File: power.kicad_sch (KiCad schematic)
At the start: 44 parts, among them U14 BH-18650-B5BA016, U2 SS-12D10L5, U4 TPS562209DDCR, U5 FXL0530-4R7-M

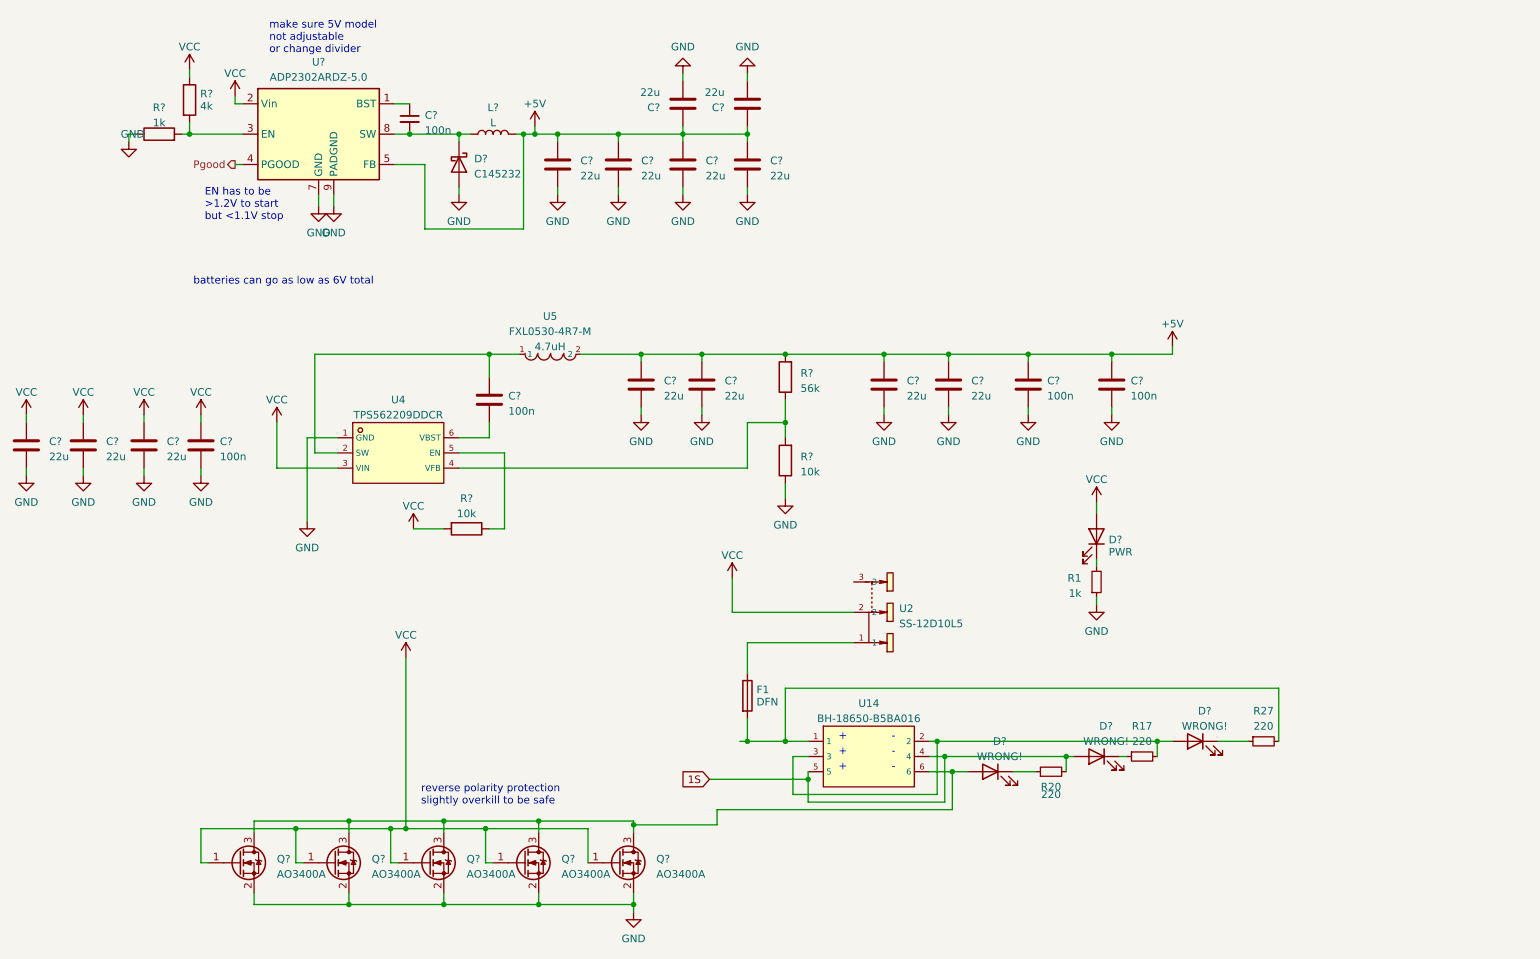
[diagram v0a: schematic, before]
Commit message: removed all dc to dc
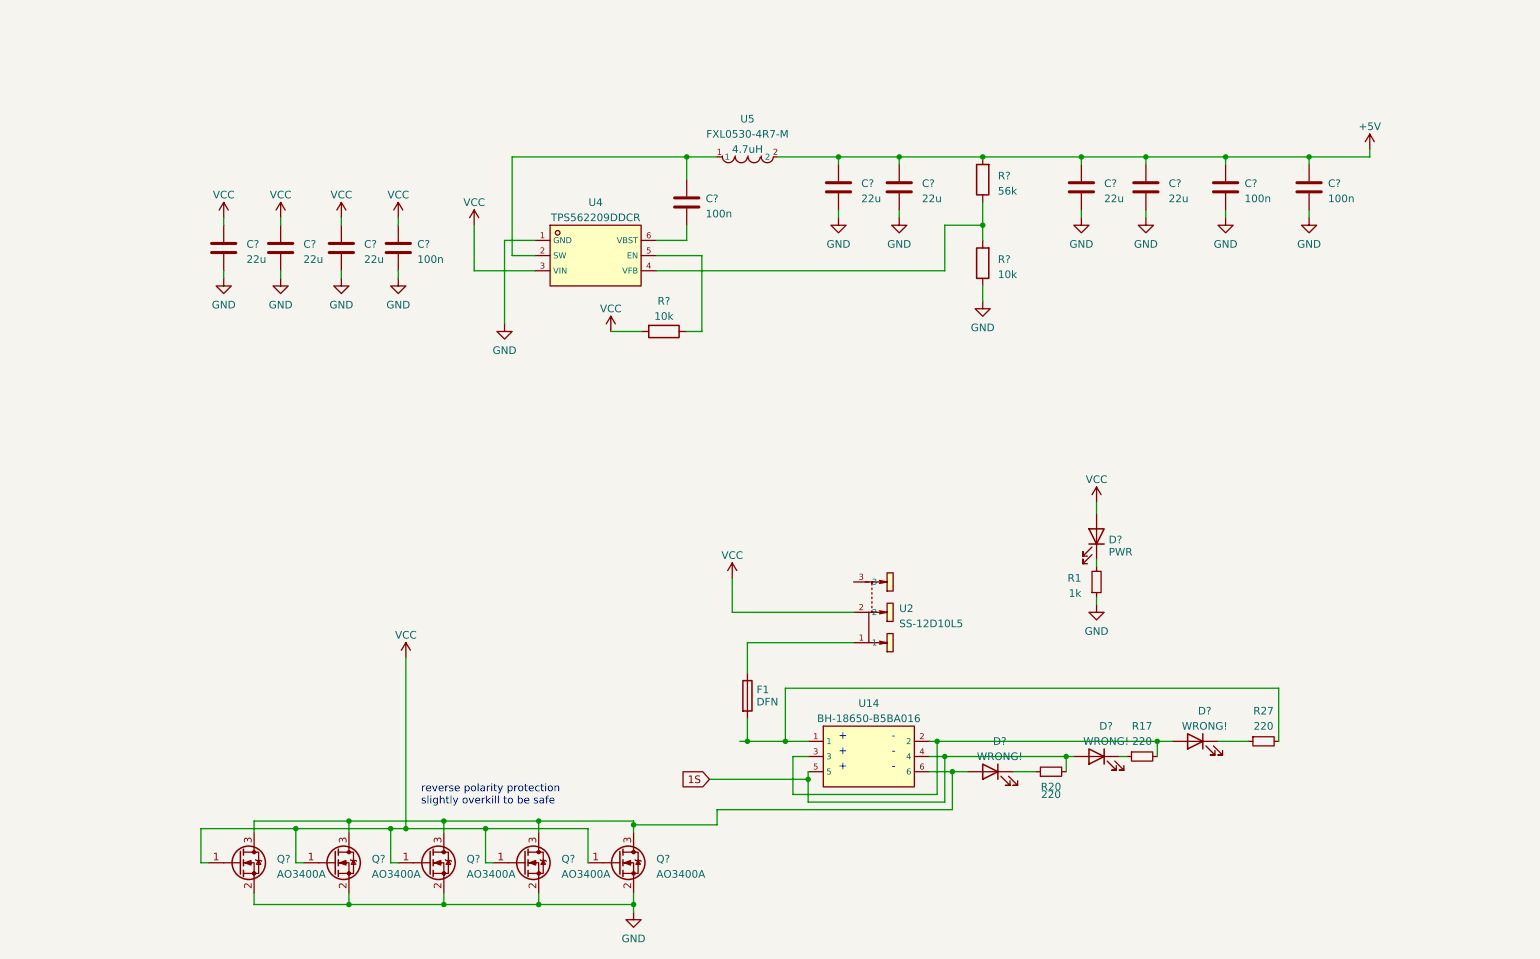
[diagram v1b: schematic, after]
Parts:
- removed C? (x6): 22u, Capacitor_SMD:C_0805_2012Metric_Pad1.18x1.45mm_HandSolder, symbol Device:C
- removed C?: 100n, Capacitor_SMD:C_0603_1608Metric_Pad1.08x0.95mm_HandSolder, symbol Device:C_Small
- removed D?: C145232, Diode_SMD:D_SMA_Handsoldering, symbol Device:D_Schottky
- removed L?: L, Inductor_SMD:L_Changjiang_FNR6045S, symbol Device:L
- removed R?: 4k, Resistor_SMD:R_0603_1608Metric_Pad0.98x0.95mm_HandSolder, symbol Device:R
- removed R?: 1k, Resistor_SMD:R_0603_1608Metric_Pad0.98x0.95mm_HandSolder, symbol Device:R
- removed U?: ADP2302ARDZ-5.0, Package_SO:SOIC-8-1EP_3.9x4.9mm_P1.27mm_EP2.29x3mm, symbol Regulator_Switching:ADP2302ARDZ-5.0
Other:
- note removed: "EN has to be >1.2V to start but <1.1V stop"
- note removed: "batteries can go as low as 6V total"
- note removed: "make sure 5V model not adjustable or change divider"
- moved on the sheet: C?, R?, U4, U5

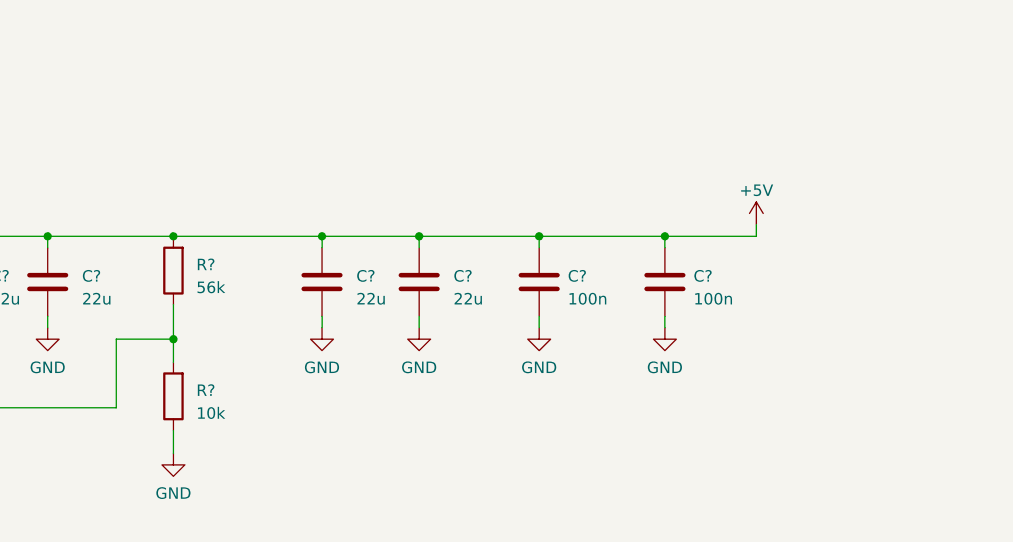
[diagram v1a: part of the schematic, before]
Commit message: Added thing for servo pwoer
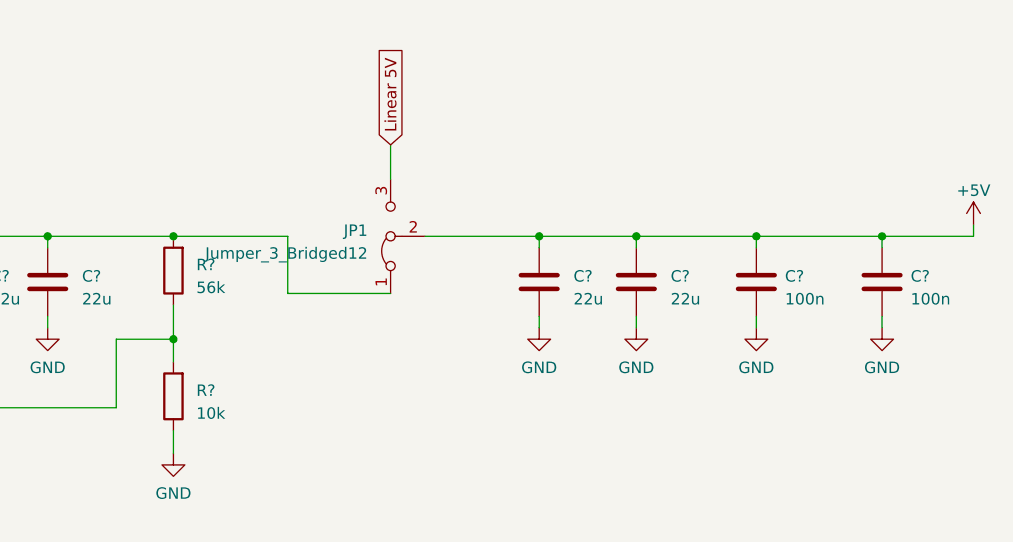
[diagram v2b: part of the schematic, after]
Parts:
- added JP1: Jumper_3_Bridged12, Jumper:SolderJumper-3_P1.3mm_Bridged12_RoundedPad1.0x1.5mm, symbol Jumper:Jumper_3_Bridged12
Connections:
- net +5V: now also JP1.2 (C); no longer C?.1, C?.1, R?.2, U5.2
- new net: C?.1, C?.1, JP1.1 (A), R?.2, U5.2
- new net Linear 5V: JP1.3 (B)
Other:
- moved on the sheet: C?

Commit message: big layout changes
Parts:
- removed U14: BH-18650-B5BA016, footprint:BAT-SMD_BH-18650-B5BA016, symbol BH-18650-B5BA016:BH-18650-B5BA016
- added U6: BH-18650-B5BA016, footprint:BAT-SMD_BH-18650-B5BA016, symbol BH-18650-B5BA016:BH-18650-B5BA016
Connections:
- net 1S: now also U6.3, U6.6
- net at D?.2 (A), Q?.3 (D), Q?.3 (D)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: now also U6.5
- net at D?.2 (A), R17.2: now also U6.1, U6.4
- net at F1.2, R27.2: now also U6.2

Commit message: 4 layer
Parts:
- removed F1: DFN, Fuse:Fuse_1210_3225Metric_Pad1.42x2.65mm_HandSolder, symbol Device:Fuse
- removed U2: SS-12D10L5, footprint:SW-TH_SS-12D10L5, symbol my_symbols:SS-12D10L5
- added F2: SMD2920B500TF, footprint:F2920, symbol my_symbols:SMD2920B500TF
- added R? (x2): 100k, Resistor_SMD:R_0603_1608Metric_Pad0.98x0.95mm_HandSolder, symbol Device:R
- added U7: 2AD1T1A2M2QES, footprint:SW-TH_2AD1T1A2M2QES, symbol my_symbols:2AD1T1A2M2QES
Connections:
- net GND: now also R?.1
- net VCC: now also R?.1, U7.1, U7.4; no longer Q?.1 (G), Q?.1 (G), Q?.1 (G), Q?.1 (G), Q?.1 (G)
- net at R27.2, U6.2: now also F2.1
- new net: Q?.1 (G), Q?.1 (G), Q?.1 (G), Q?.1 (G), Q?.1 (G), R?.2, R?.2
- new net: F2.2, U7.2, U7.5
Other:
- note added: "dividing in half to stay in spec of gate voltage"
